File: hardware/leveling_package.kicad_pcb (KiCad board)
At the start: 2 copper layers, 100 x 100 mm, 3 parts, among them J1 Conn_01x16_Male, J2 Conn_01x16_Male

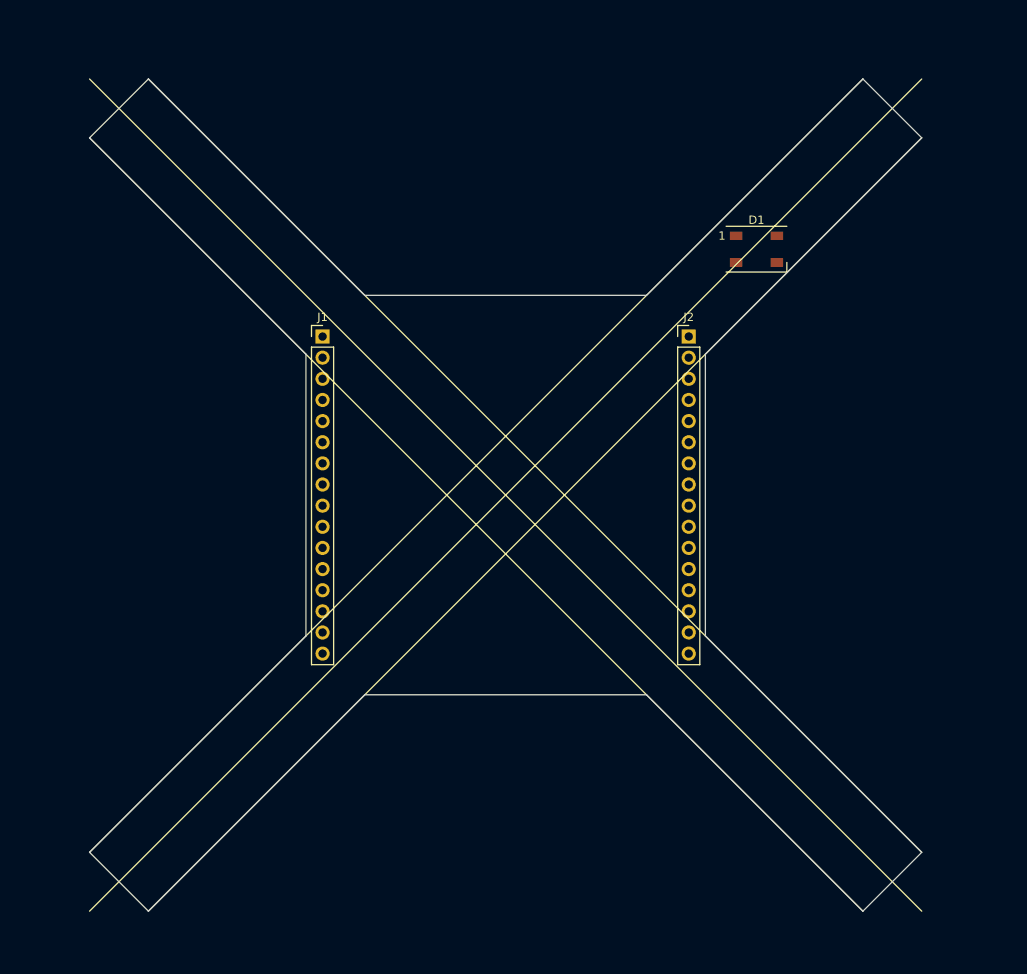
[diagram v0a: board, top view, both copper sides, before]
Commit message: first leg with all leds
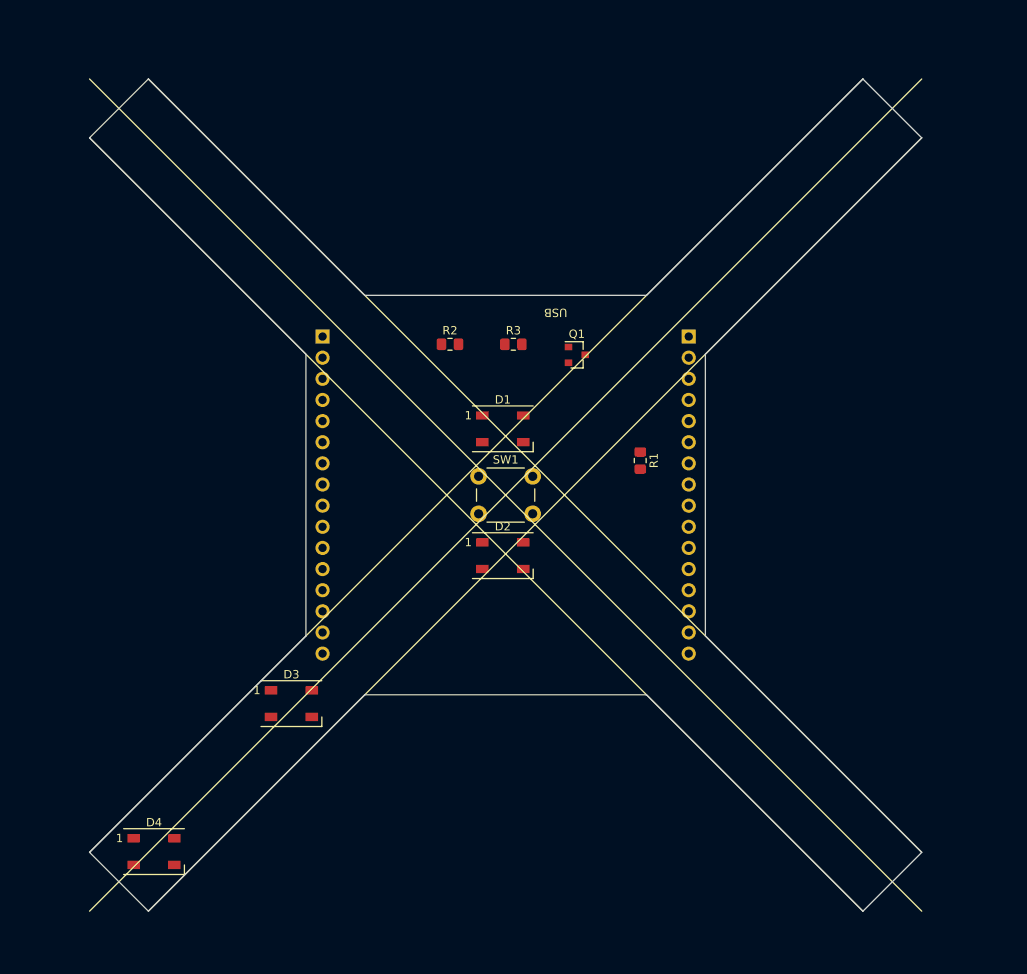
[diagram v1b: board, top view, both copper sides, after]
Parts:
- added D2: WS2812B, LED_SMD:LED_WS2812B_PLCC4_5.0x5.0mm_P3.2mm, F.Cu at (73.7, 81.3)
- added D3: WS2812B, LED_SMD:LED_WS2812B_PLCC4_5.0x5.0mm_P3.2mm, F.Cu at (48.3, 99.1)
- added D4: WS2812B, LED_SMD:LED_WS2812B_PLCC4_5.0x5.0mm_P3.2mm, F.Cu at (31.8, 116.8)
- added Q1: BSS138, Package_TO_SOT_SMD:SOT-23, F.Cu at (82.5, 57.1)
- added R1: R, Resistor_SMD:R_0805_2012Metric_Pad1.15x1.40mm_HandSolder, F.Cu at (90.2, 69.8)
- added R2: R, Resistor_SMD:R_0805_2012Metric_Pad1.15x1.40mm_HandSolder, F.Cu at (67.3, 55.9)
- added R3: R, Resistor_SMD:R_0805_2012Metric_Pad1.15x1.40mm_HandSolder, F.Cu at (74.9, 55.9)
- added SW1: SW_Push, Button_Switch_THT:SW_PUSH_6mm, F.Cu at (70.8, 71.8)
- J1: renamed from J2; moved to B.Cu
- J2: renamed from J1; moved to B.Cu
- moved D1 37.4 mm to (73.7, 66.0)
- turned J1 to 180 degrees
- turned J2 to 180 degrees
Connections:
- J2 pad 1: Net-(J1-Pad1) (its old number) -> Net-(D1-Pad1)
- J2 pad 2: Net-(J1-Pad2) (its old number) -> Net-(D1-Pad3)
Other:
- board text added: "USB"

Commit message: all legs with leds
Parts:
- added D10: WS2812B, LED_SMD:LED_WS2812B_PLCC4_5.0x5.0mm_P3.2mm, F.Cu at (116.8, 30.5)
- added D5: WS2812B, LED_SMD:LED_WS2812B_PLCC4_5.0x5.0mm_P3.2mm, F.Cu at (100.3, 99.1)
- added D6: WS2812B, LED_SMD:LED_WS2812B_PLCC4_5.0x5.0mm_P3.2mm, F.Cu at (116.8, 116.8)
- added D7: WS2812B, LED_SMD:LED_WS2812B_PLCC4_5.0x5.0mm_P3.2mm, F.Cu at (44.5, 44.5)
- added D8: WS2812B, LED_SMD:LED_WS2812B_PLCC4_5.0x5.0mm_P3.2mm, F.Cu at (31.8, 30.5)
- added D9: WS2812B, LED_SMD:LED_WS2812B_PLCC4_5.0x5.0mm_P3.2mm, F.Cu at (104.1, 44.5)

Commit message: firmware tests neopix
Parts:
- added D11: WS2812B, LED_SMD:LED_WS2812B_PLCC4_5.0x5.0mm_P3.2mm, F.Cu at (116.8, 30.5)
- moved D7 102.4 mm to (116.8, 116.8)
- moved D9 73.5 mm to (31.8, 31.8)
- moved D5 72.1 mm to (30.5, 116.8)
- moved D3 30.3 mm to (73.7, 82.5)
- moved D10 23.3 mm to (100.3, 47.0)
- moved D4 23.3 mm to (48.3, 100.3)
- moved D6 22.5 mm to (101.6, 100.3)
- moved D8 20.7 mm to (45.7, 45.7)
- moved D1 19.8 mm to (87.6, 80.0)
- moved D2 16.5 mm to (73.7, 64.8)
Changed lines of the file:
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@@
     (tracks 0)
     (zones 0)
-    (modules 17)
-    (nets 44)
+    (modules 18)
+    (nets 45)
   )
   (page A4)
@@
   (net 42 "Net-(D10-Pad4)")
   (net 43 "Net-(D10-Pad2)")
+  (net 44 "Net-(D11-Pad2)")
   (net_class Default "This is the default net class."
     (clearance 0.2)
@@
     (add_net "Net-(D10-Pad2)")
     (add_net "Net-(D10-Pad4)")
+    (add_net "Net-(D11-Pad2)")
     (add_net "Net-(D2-Pad2)")
     (add_net "Net-(D3-Pad2)")
@@
     (tags "LED RGB NeoPixel")
     (attr smd)
+    (fp_text reference D11 (at 0 -3.5) (layer F.SilkS)
+      (effects (font (size 1 1) (thickness 0.15)))
+    )
+    (fp_text value WS2812B (at 0 4) (layer F.Fab)
+      (effects (font (size 1 1) (thickness 0.15)))
+    )
+    (fp_circle (center 0 0) (end 0 -2) (layer F.Fab) (width 0.1))
+    (fp_line (start 3.65 2.75) (end 3.65 1.6) (layer F.SilkS) (width 0.12))
+    (fp_line (start -3.65 2.75) (end 3.65 2.75) (layer F.SilkS) (width 0.12))
+    (fp_line (start -3.65 -2.75) (end 3.65 -2.75) (layer F.SilkS) (width 0.12))
+    (fp_line (start 2.5 -2.5) (end -2.5 -2.5) (layer F.Fab) (width 0.1))
+    (fp_line (start 2.5 2.5) (end 2.5 -2.5) (layer F.Fab) (width 0.1))
+    (fp_line (start -2.5 2.5) (end 2.5 2.5) (layer F.Fab) (width 0.1))
+    (fp_line (start -2.5 -2.5) (end -2.5 2.5) (layer F.Fab) (width 0.1))
+    (fp_line (start 2.5 1.5) (end 1.5 2.5) (layer F.Fab) (width 0.1))
+    (fp_line (start -3.45 -2.75) (end -3.45 2.75) (layer F.CrtYd) (width 0.05))
+    (fp_line (start -3.45 2.75) (end 3.45 2.75) (layer F.CrtYd) (width 0.05))
+    (fp_line (start 3.45 2.75) (end 3.45 -2.75) (layer F.CrtYd) (width 0.05))
+    (fp_line (start 3.45 -2.75) (end -3.45 -2.75) (layer F.CrtYd) (width 0.05))
+    (fp_text user %R (at 0 0) (layer F.Fab)
+      (effects (font (size 0.8 0.8) (thickness 0.15)))
+    )
+    (fp_text user 1 (at -4.15 -1.6) (layer F.SilkS)
+      (effects (font (size 1 1) (thickness 0.15)))
+    )
+    (pad 1 smd rect (at -2.45 -1.6) (size 1.5 1) (layers F.Cu F.Paste F.Mask)
+      (net 31 "Net-(D1-Pad1)"))
+    (pad 2 smd rect (at -2.45 1.6) (size 1.5 1) (layers F.Cu F.Paste F.Mask)
+      (net 44 "Net-(D11-Pad2)"))
+    (pad 4 smd rect (at 2.45 -1.6) (size 1.5 1) (layers F.Cu F.Paste F.Mask)
+      (net 43 "Net-(D10-Pad2)"))
+    (pad 3 smd rect (at 2.45 1.6) (size 1.5 1) (layers F.Cu F.Paste F.Mask)
+      (net 34 "Net-(D1-Pad3)"))
+    (model ${KISYS3DMOD}/LED_SMD.3dshapes/LED_WS2812B_PLCC4_5.0x5.0mm_P3.2mm.wrl
+      (at (xyz 0 0 0))
+      (scale (xyz 1 1 1))
+      (rotate (xyz 0 0 0))
+    )
+  )
+  (module LED_SMD:LED_WS2812B_PLCC4_5.0x5.0mm_P3.2mm (layer F.Cu)
+    (at 100.33 46.99)
+    (descr https://cdn-shop.adafruit.com/datasheets/WS2812B.pdf)
+    (tags "LED RGB NeoPixel")
+    (attr smd)
     (fp_text reference D10 (at 0 -3.5) (layer F.SilkS)
       (effects (font (size 1 1) (thickness 0.15)))
@@
   )
   (module LED_SMD:LED_WS2812B_PLCC4_5.0x5.0mm_P3.2mm (layer F.Cu)
-    (at 104.14 44.45)
+    (at 31.75 31.75)
     (descr https://cdn-shop.adafruit.com/datasheets/WS2812B.pdf)
     (tags "LED RGB NeoPixel")
@@
   )
   (module LED_SMD:LED_WS2812B_PLCC4_5.0x5.0mm_P3.2mm (layer F.Cu)
-    (at 31.75 30.48)
+    (at 45.72 45.72)
     (descr https://cdn-shop.adafruit.com/datasheets/WS2812B.pdf)
     (tags "LED RGB NeoPixel")
@@
   )
   (module LED_SMD:LED_WS2812B_PLCC4_5.0x5.0mm_P3.2mm (layer F.Cu)
-    (at 44.45 44.45)
+    (at 116.84 116.84)
     (descr https://cdn-shop.adafruit.com/datasheets/WS2812B.pdf)
     (tags "LED RGB NeoPixel")
@@
   )
   (module LED_SMD:LED_WS2812B_PLCC4_5.0x5.0mm_P3.2mm (layer F.Cu)
-    (at 116.84 116.84)
+    (at 101.6 100.33)
     (descr https://cdn-shop.adafruit.com/datasheets/WS2812B.pdf)
     (tags "LED RGB NeoPixel")
@@
   )
   (module LED_SMD:LED_WS2812B_PLCC4_5.0x5.0mm_P3.2mm (layer F.Cu)
-    (at 100.33 99.06)
+    (at 30.48 116.84)
     (descr https://cdn-shop.adafruit.com/datasheets/WS2812B.pdf)
     (tags "LED RGB NeoPixel")
@@
   )
   (module LED_SMD:LED_WS2812B_PLCC4_5.0x5.0mm_P3.2mm (layer F.Cu)
-    (at 31.75 116.84)
+    (at 48.26 100.33)
     (descr https://cdn-shop.adafruit.com/datasheets/WS2812B.pdf)
     (tags "LED RGB NeoPixel")
@@
   )
   (module LED_SMD:LED_WS2812B_PLCC4_5.0x5.0mm_P3.2mm (layer F.Cu)
-    (at 48.26 99.06)
+    (at 73.66 82.55)
     (descr https://cdn-shop.adafruit.com/datasheets/WS2812B.pdf)
     (tags "LED RGB NeoPixel")
@@
   )
   (module LED_SMD:LED_WS2812B_PLCC4_5.0x5.0mm_P3.2mm (layer F.Cu)
-    (at 73.66 81.28)
+    (at 73.66 64.77)
     (descr https://cdn-shop.adafruit.com/datasheets/WS2812B.pdf)
     (tags "LED RGB NeoPixel")
@@
   )
   (module LED_SMD:LED_WS2812B_PLCC4_5.0x5.0mm_P3.2mm (layer F.Cu)
-    (at 73.66 66.04)
-    (descr https://cdn-shop.adafruit.com/datasheets/WS2812B.pdf)
-    (tags "LED RGB NeoPixel")
+    (at 87.63 80.01)
+    (descr https://cdn-shop.adafruit.com/datasheets/WS2812B.pdf)
+    (tags "LED RGB NeoPixel")

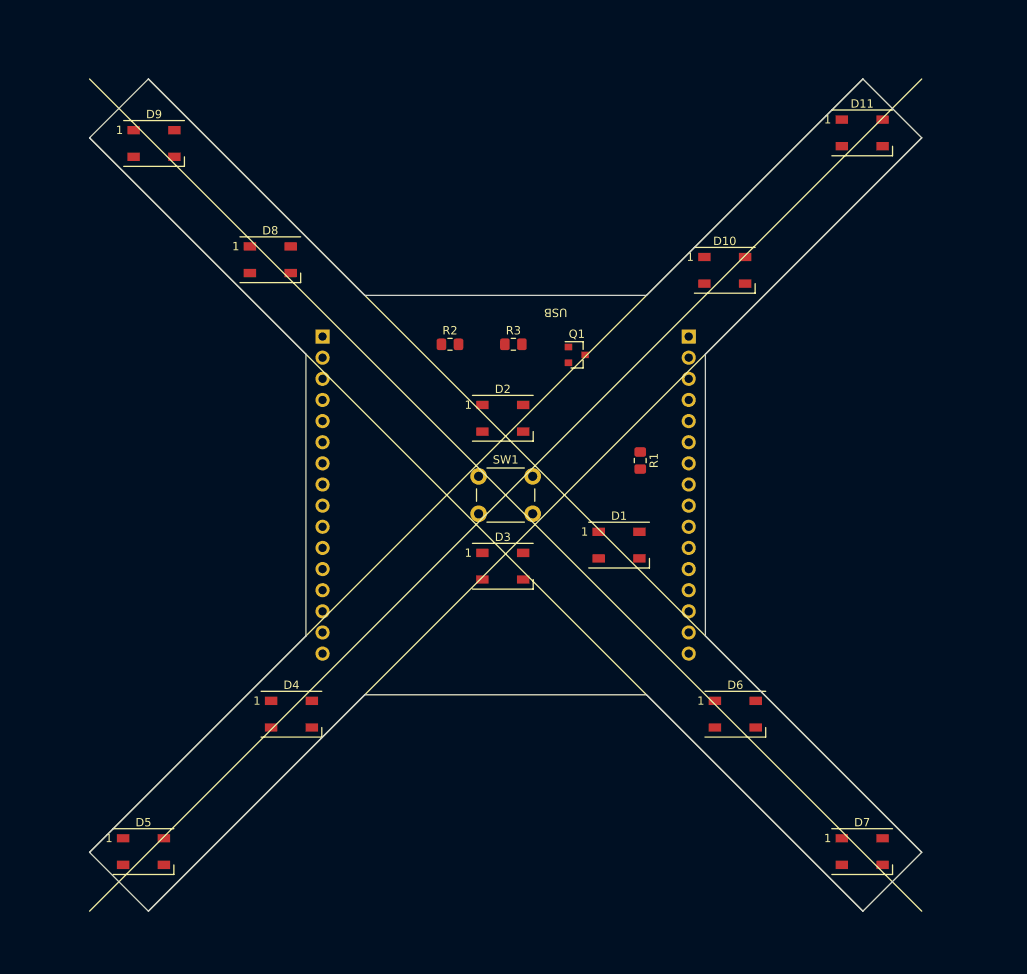
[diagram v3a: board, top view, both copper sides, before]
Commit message: all traces routed
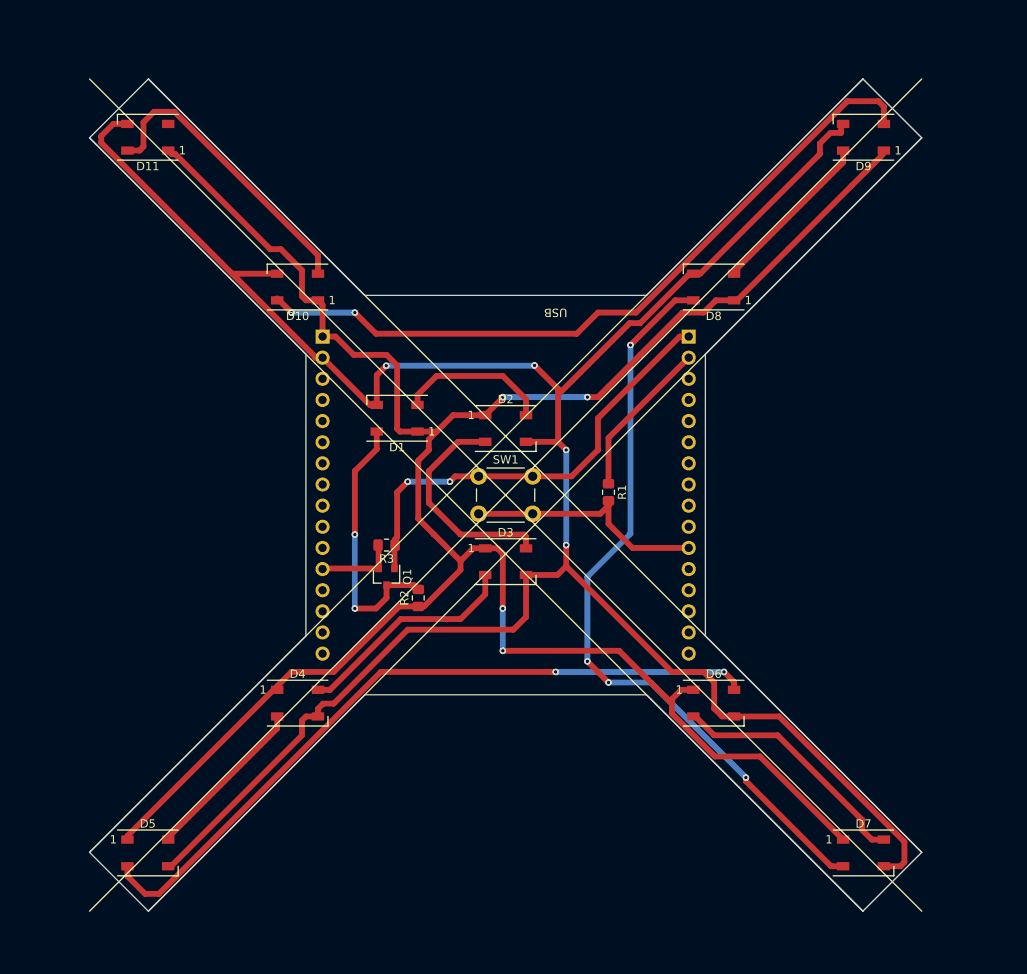
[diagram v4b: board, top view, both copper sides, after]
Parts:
- moved D11 85.8 mm to (31.0, 31.0), turned to 180 degrees
- moved D9 85.3 mm to (117.0, 31.0), turned to 180 degrees
- moved D8 53.4 mm to (99.0, 49.0), turned to 180 degrees
- moved D10 51.4 mm to (49.0, 49.0), turned to 180 degrees
- moved Q1 35.1 mm to (59.7, 83.8), turned to 270 degrees
- moved D1 30.7 mm to (61.0, 64.8), turned to 180 degrees
- moved R2 30.7 mm to (63.5, 86.4), turned to 90 degrees
- moved R3 28.5 mm to (59.7, 80.0), turned to 180 degrees
- moved R1 5.39 mm to (86.4, 73.7)
- moved D6 2.92 mm to (99.0, 99.0)
- moved D4 1.52 mm to (49.0, 99.0)
- moved D2 1.28 mm to (74.0, 66.0)
- moved D3 0.65 mm to (74.0, 82.0)
- moved D5 0.54 mm to (31.0, 117.0)
- moved D7 0.23 mm to (117.0, 117.0)
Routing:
- net Net-(D1-Pad3): track 0.00 -> 286.3 mm, vias 0 -> 4
- net Net-(D1-Pad1): track 0.00 -> 268.4 mm, vias 0 -> 4
- net Net-(D7-Pad2): track 0.00 -> 91.1 mm, vias 0 -> 4
- net Net-(D10-Pad4): track 0.00 -> 88.7 mm, vias 0 -> 2
- net Net-(D5-Pad2): track 0.00 -> 87.6 mm, vias 0 -> 2
- net Net-(J1-Pad1): track 0.00 -> 54.3 mm, vias 0 -> 2
- net Net-(D10-Pad2): track 0.00 -> 35.9 mm
- net Net-(D1-Pad4): track 0.00 -> 32.2 mm, vias 0 -> 2
- net Net-(J1-Pad11): track 0.00 -> 30.2 mm
- net Net-(D6-Pad2): track 0.00 -> 29.7 mm
- net Net-(D3-Pad2): track 0.00 -> 27.2 mm
- net Net-(D2-Pad2): track 0.00 -> 26.8 mm
- net Net-(D4-Pad2): track 0.00 -> 20.2 mm
- net Net-(D8-Pad2): track 0.00 -> 20.2 mm
- net Net-(J1-Pad2): track 0.00 -> 19.1 mm
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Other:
- net class Default: trace_width 0.25 -> 0.7

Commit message: legs a bit wider
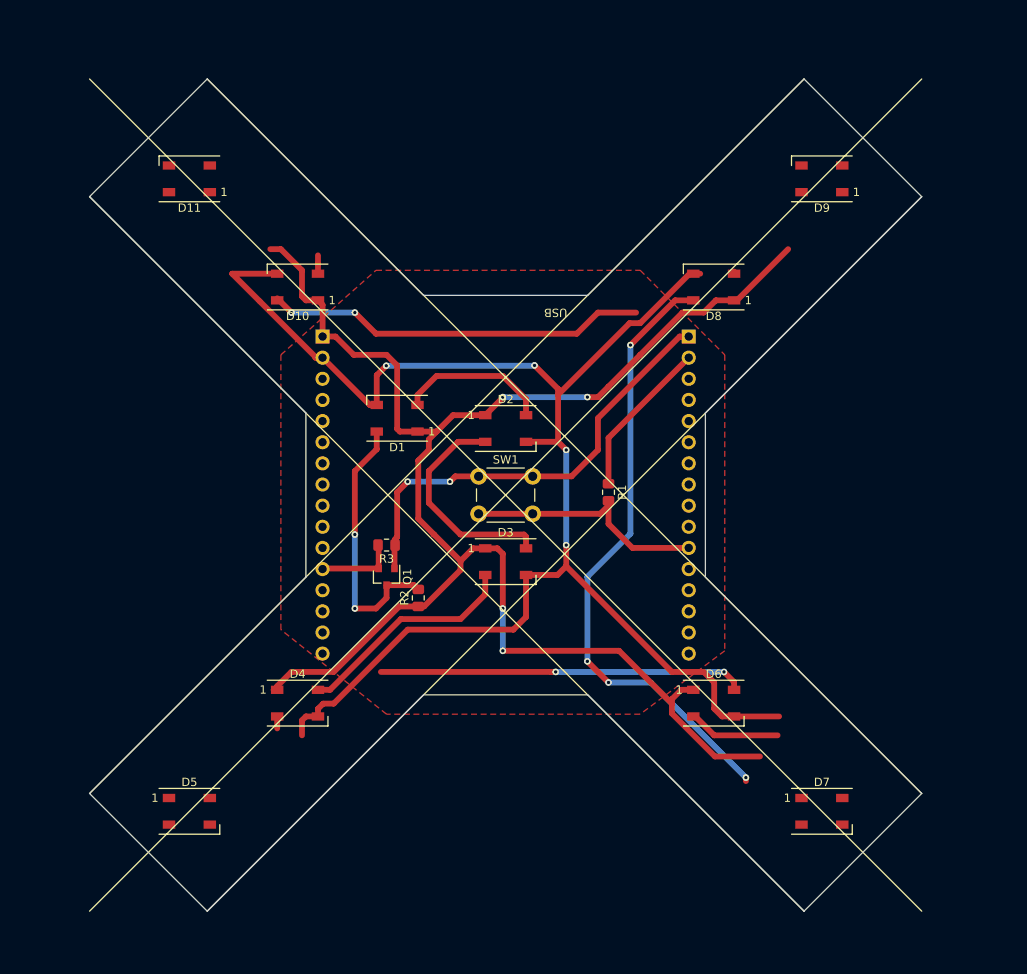
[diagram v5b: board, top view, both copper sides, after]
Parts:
- moved D11 7.07 mm to (36.0, 36.0)
- moved D5 7.07 mm to (36.0, 112.0)
- moved D7 7.07 mm to (112.0, 112.0)
- moved D9 7.07 mm to (112.0, 36.0)
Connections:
- J1 pad 2: Net-(J1-Pad2) -> Net-(D1-Pad3)
- R1 pad 1: Net-(J1-Pad2) -> Net-(D1-Pad3)
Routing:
- net Net-(D1-Pad3): track 286.3 -> 203.8 mm
- net Net-(D1-Pad1): track 268.4 -> 195.7 mm
- net Net-(D5-Pad2): track 87.6 -> 44.0 mm
- net Net-(D10-Pad4): track 88.7 -> 46.1 mm
- net Net-(D10-Pad2): track 35.9 -> 2.21 mm
- net Net-(D8-Pad2): track 20.2 -> 0.26 mm
- net Net-(J1-Pad2): track 19.1 -> 0.00 mm
- net Net-(D4-Pad2): track 20.2 -> 1.44 mm
- net Net-(D6-Pad2): track 29.7 -> 11.1 mm
- net Net-(D7-Pad2): track 91.1 -> 75.2 mm
- added copper zone on F.Cu, net Net-(D1-Pad3)
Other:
- outline, holes or cut-outs redrawn

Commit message: added proto solder pads
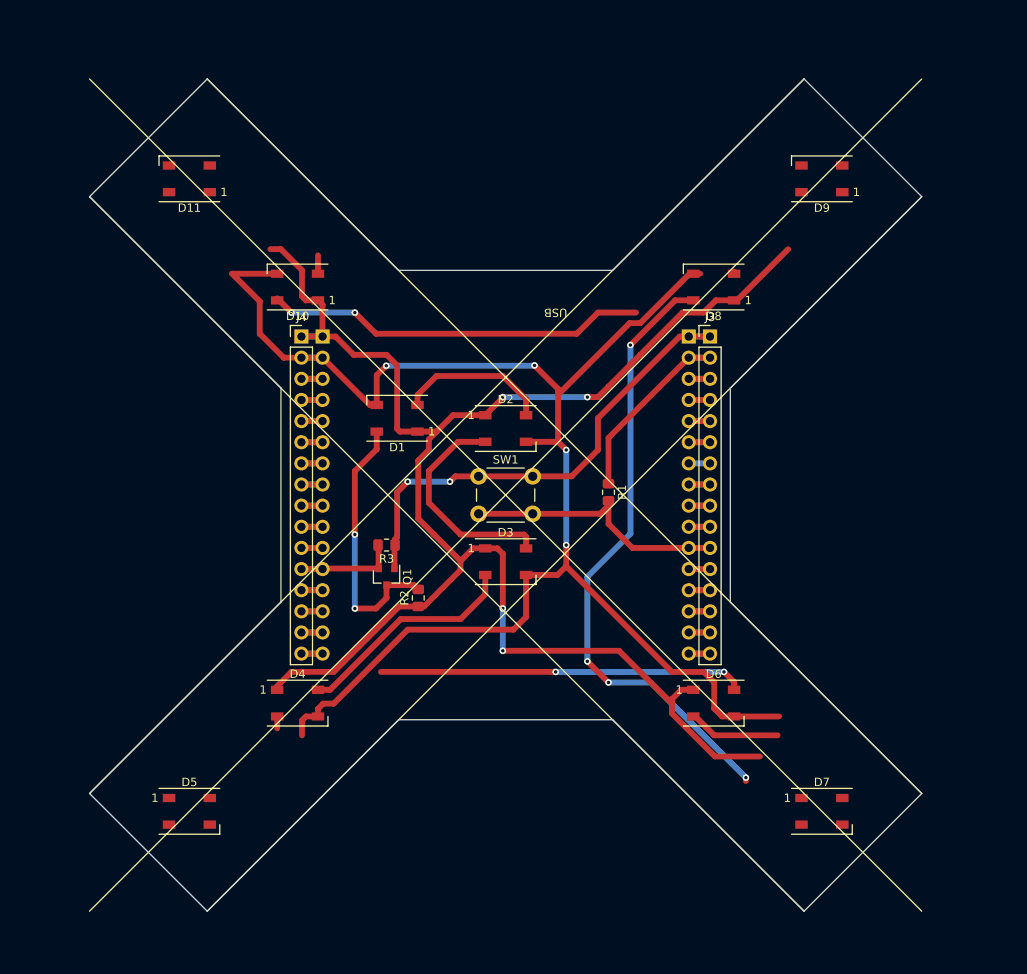
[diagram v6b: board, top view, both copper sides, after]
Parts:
- added J3: Conn_01x16_Male, Connector_PinHeader_2.54mm:PinHeader_1x16_P2.54mm_Vertical, F.Cu at (98.6, 55.0)
- added J4: Conn_01x16_Male, Connector_PinHeader_2.54mm:PinHeader_1x16_P2.54mm_Vertical, F.Cu at (49.5, 55.0)
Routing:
- net Net-(D1-Pad3): track 203.8 -> 213.7 mm
- net Net-(J1-Pad11): track 30.2 -> 35.3 mm
- net Net-(J1-Pad9): track 0.00 -> 5.12 mm
- net Net-(J1-Pad8): track 0.00 -> 5.12 mm
- net Net-(J1-Pad6): track 0.00 -> 5.12 mm
- net Net-(J1-Pad5): track 0.00 -> 5.12 mm
- net Net-(J1-Pad4): track 0.00 -> 5.12 mm
- net Net-(J1-Pad3): track 0.00 -> 5.12 mm
- net Net-(J1-Pad16): track 0.00 -> 5.12 mm
- net Net-(J1-Pad15): track 0.00 -> 5.12 mm
- net Net-(J1-Pad14): track 0.00 -> 5.12 mm
- net Net-(J1-Pad13): track 0.00 -> 5.12 mm
- net Net-(J1-Pad12): track 0.00 -> 5.12 mm
- net Net-(J1-Pad10): track 0.00 -> 5.12 mm
- net Net-(J1-Pad1): track 54.3 -> 59.4 mm
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- removed copper zone on F.Cu, net Net-(D1-Pad3)
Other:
- outline, holes or cut-outs redrawn
